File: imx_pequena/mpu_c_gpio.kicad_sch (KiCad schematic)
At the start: 1 part, among them U1 MCIMX6Z0DVM09AB

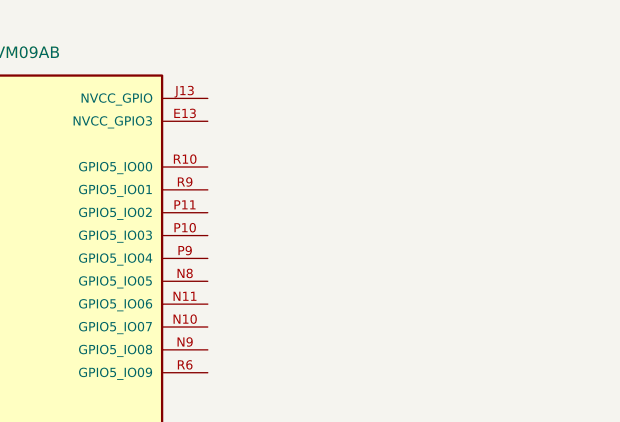
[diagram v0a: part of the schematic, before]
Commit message: Cleaned up NVCC pins
Added 3v3 connections + decoupling caps to NVcc pins
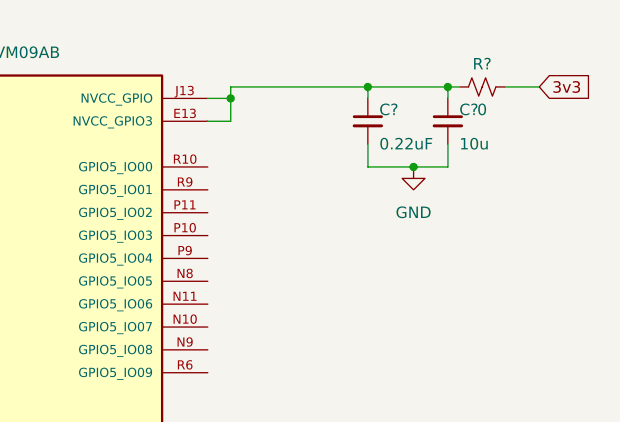
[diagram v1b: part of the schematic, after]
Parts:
- added C?: 10u, symbol Device:C_Small
- added C?: 0.22uF, symbol Device:C_Small
- added R?: 0, symbol Device:R_Small_US
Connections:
- net at U1.E13 (NVCC_GPIO3): now also U1.J13 (NVCC_GPIO), C?.1, C?.1, R?.1
- new net 3v3: R?.2
- new net GND: C?.2, C?.2
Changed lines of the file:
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@@
 (kicad_sch (version 20211123) (generator eeschema)
   (paper "A4")
+  (junction (at 185.42 48.26) (diameter 0) (color 0 0 0 0)
+  )
+  (junction (at 165.1 40.64) (diameter 0) (color 0 0 0 0)
+  )
+  (junction (at 180.34 39.37) (diameter 0) (color 0 0 0 0)
+  )
+  (junction (at 189.23 39.37) (diameter 0) (color 0 0 0 0)
+  )
+  (wire (pts (xy 189.23 39.37) (xy 189.23 40.64))
+    (stroke (width 0) (type default) (color 0 0 0 0))
+  )
+  (wire (pts (xy 165.1 40.64) (xy 165.1 39.37))
+    (stroke (width 0) (type default) (color 0 0 0 0))
+  )
+  (wire (pts (xy 165.1 39.37) (xy 180.34 39.37))
+    (stroke (width 0) (type default) (color 0 0 0 0))
+  )
+  (wire (pts (xy 165.1 43.18) (xy 165.1 40.64))
+    (stroke (width 0) (type default) (color 0 0 0 0))
+  )
+  (wire (pts (xy 189.23 45.72) (xy 189.23 48.26))
+    (stroke (width 0) (type default) (color 0 0 0 0))
+  )
+  (wire (pts (xy 180.34 39.37) (xy 189.23 39.37))
+    (stroke (width 0) (type default) (color 0 0 0 0))
+  )
+  (wire (pts (xy 180.34 45.72) (xy 180.34 48.26))
+    (stroke (width 0) (type default) (color 0 0 0 0))
+  )
+  (wire (pts (xy 189.23 39.37) (xy 190.5 39.37))
+    (stroke (width 0) (type default) (color 0 0 0 0))
+  )
+  (wire (pts (xy 185.42 48.26) (xy 189.23 48.26))
+    (stroke (width 0) (type default) (color 0 0 0 0))
+  )
+  (wire (pts (xy 162.56 40.64) (xy 165.1 40.64))
+    (stroke (width 0) (type default) (color 0 0 0 0))
+  )
+  (wire (pts (xy 180.34 39.37) (xy 180.34 40.64))
+    (stroke (width 0) (type default) (color 0 0 0 0))
+  )
+  (wire (pts (xy 180.34 48.26) (xy 185.42 48.26))
+    (stroke (width 0) (type default) (color 0 0 0 0))
+  )
+  (wire (pts (xy 195.58 39.37) (xy 199.39 39.37))
+    (stroke (width 0) (type default) (color 0 0 0 0))
+  )
+  (wire (pts (xy 162.56 43.18) (xy 165.1 43.18))
+    (stroke (width 0) (type default) (color 0 0 0 0))
+  )
+  (global_label "3v3" (shape input) (at 199.39 39.37 0) (fields_autoplaced)
+    (effects (font (size 1.27 1.27)) (justify left))
+    (property "Intersheet References" "${INTERSHEET_REFS}" (id 0) (at 205.1898 39.2906 0)
+      (effects (font (size 1.27 1.27)) (justify left) hide)
+    )
+  )
   (symbol (lib_id "MCIMX6Z0DVM09AB:MCIMX6Z0DVM09AB") (at 137.16 93.98 0) (unit 3)
     (in_bom yes) (on_board yes) (fields_autoplaced)
@@
     (pin "R9")
   )
+  (symbol (lib_id "Device:R_Small_US") (at 193.04 39.37 90) (unit 1)
+    (in_bom yes) (on_board yes)
+    (property "Reference" "R?" (id 0) (at 193.04 36.83 90))
+    (property "Value" "0" (id 1) (at 193.04 41.91 90))
+    (property "Footprint" "" (id 2) (at 193.04 39.37 0)
+      (effects (font (size 1.27 1.27)) hide)
+    )
+    (property "Datasheet" "~" (id 3) (at 193.04 39.37 0)
+      (effects (font (size 1.27 1.27)) hide)
+    )
+    (pin "1")
+    (pin "2")
+  )
+  (symbol (lib_id "power:GND") (at 185.42 48.26 0) (unit 1)
+    (in_bom yes) (on_board yes) (fields_autoplaced)
+    (property "Reference" "#PWR?" (id 0) (at 185.42 54.61 0)
+      (effects (font (size 1.27 1.27)) hide)
+    )
+    (property "Value" "GND" (id 1) (at 185.42 53.34 0))
+    (property "Footprint" "" (id 2) (at 185.42 48.26 0)
+      (effects (font (size 1.27 1.27)) hide)
+    )
+    (property "Datasheet" "" (id 3) (at 185.42 48.26 0)
+      (effects (font (size 1.27 1.27)) hide)
+    )
+    (pin "1")
+  )
+  (symbol (lib_id "Device:C_Small") (at 189.23 43.18 0) (unit 1)
+    (in_bom yes) (on_board yes)
+    (property "Reference" "C?" (id 0) (at 190.5 41.91 0)
+      (effects (font (size 1.27 1.27)) (justify left))
+    )
+    (property "Value" "10u" (id 1) (at 190.5 45.72 0)
+      (effects (font (size 1.27 1.27)) (justify left))
+    )
+    (property "Footprint" "" (id 2) (at 189.23 43.18 0)
+      (effects (font (size 1.27 1.27)) hide)
+    )
+    (property "Datasheet" "~" (id 3) (at 189.23 43.18 0)
+      (effects (font (size 1.27 1.27)) hide)
+    )
+    (pin "1")
+    (pin "2")
+  )
+  (symbol (lib_id "Device:C_Small") (at 180.34 43.18 0) (unit 1)
+    (in_bom yes) (on_board yes)
+    (property "Reference" "C?" (id 0) (at 181.61 41.91 0)
+      (effects (font (size 1.27 1.27)) (justify left))
+    )
+    (property "Value" "0.22uF" (id 1) (at 181.61 45.72 0)
+      (effects (font (size 1.27 1.27)) (justify left))
+    )
+    (property "Footprint" "" (id 2) (at 180.34 43.18 0)
+      (effects (font (size 1.27 1.27)) hide)
+    )
+    (property "Datasheet" "~" (id 3) (at 180.34 43.18 0)
+      (effects (font (size 1.27 1.27)) hide)
+    )
+    (pin "1")
+    (pin "2")
+  )
 )

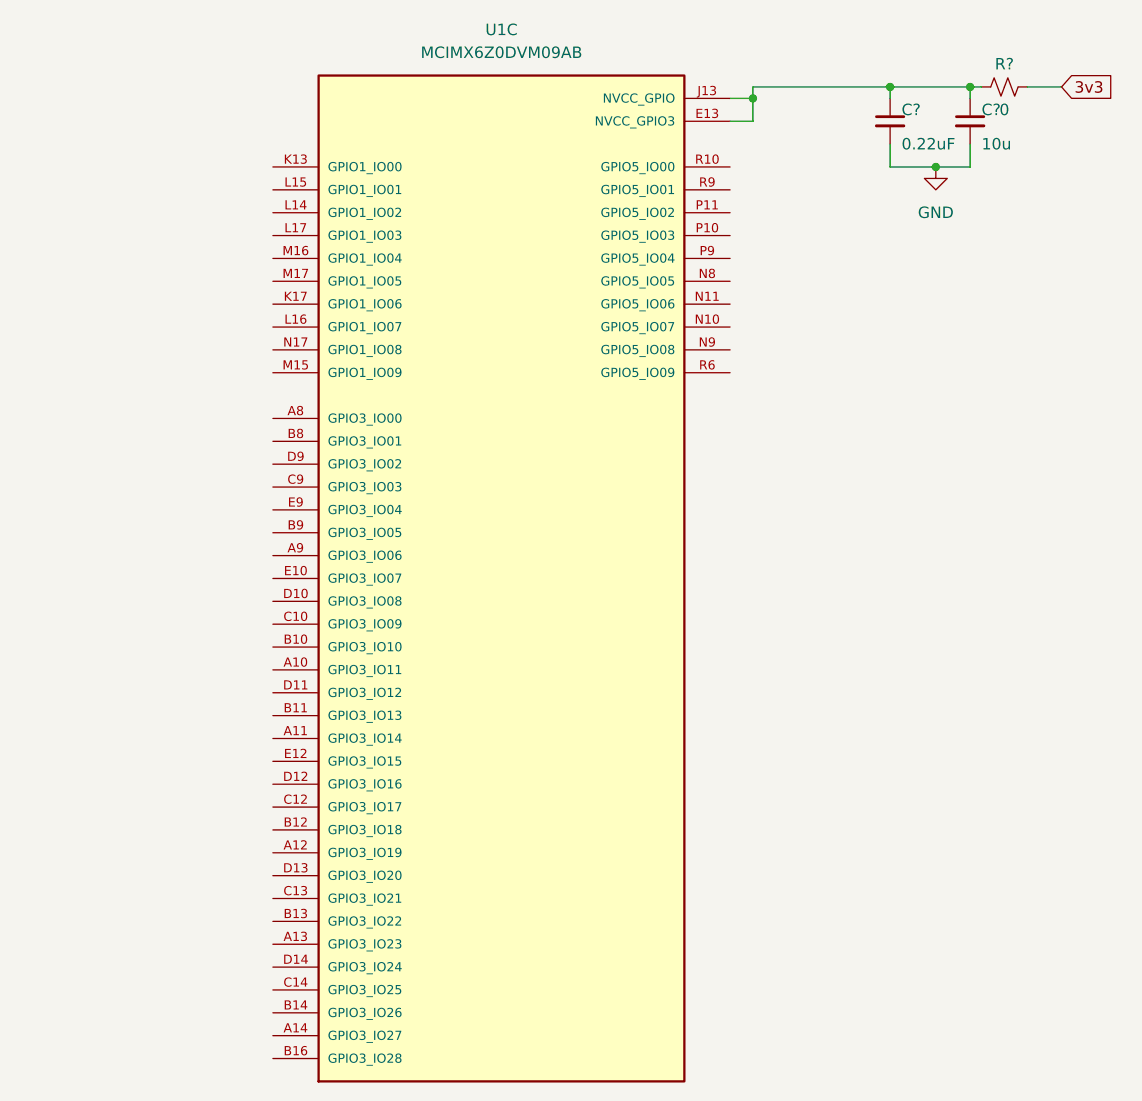
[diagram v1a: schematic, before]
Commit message: Pinout updates
Updated pinout files, changed pinout of gpio 1 and 3
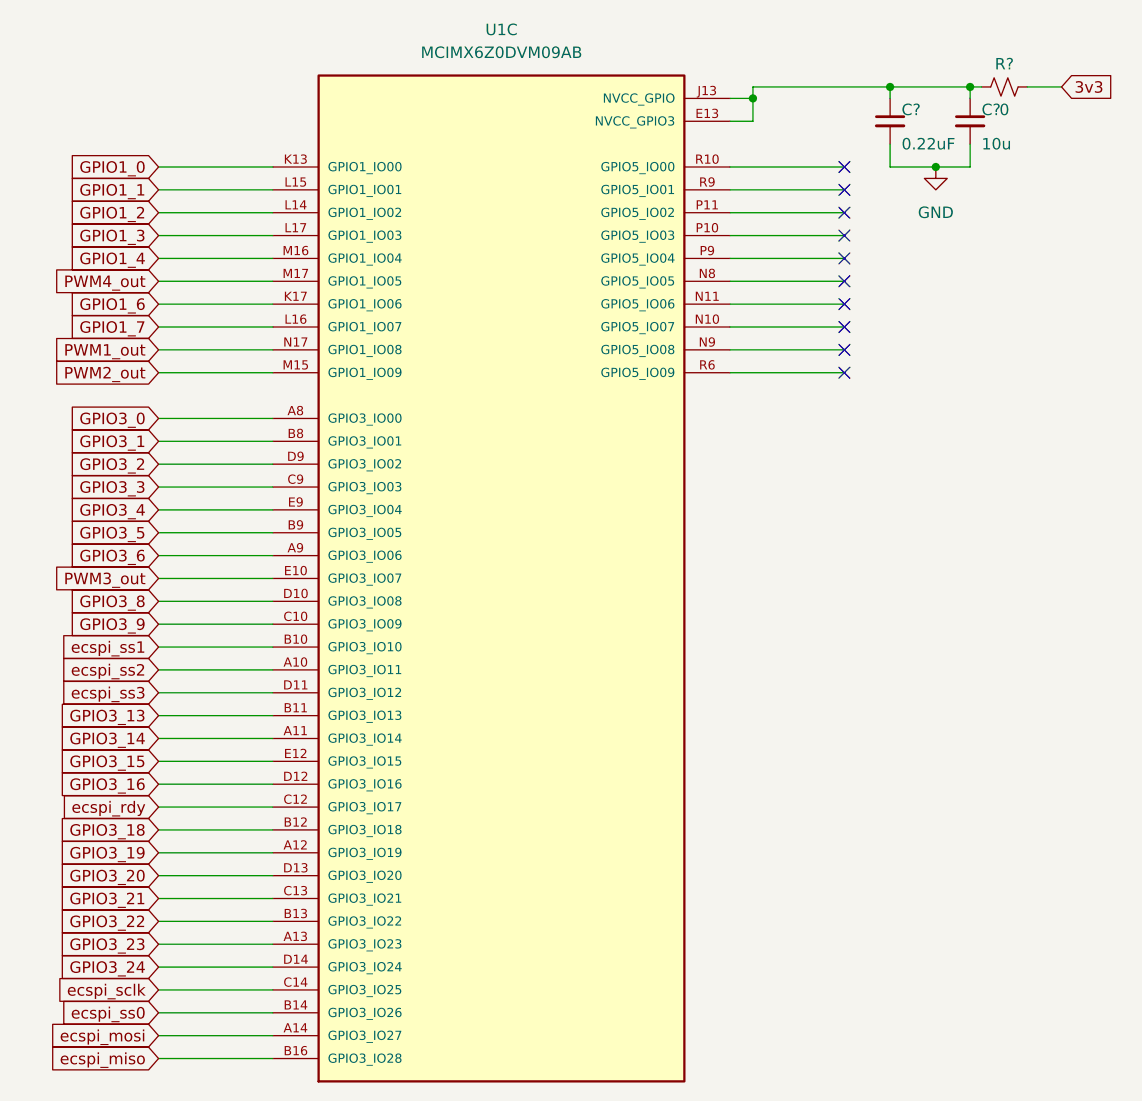
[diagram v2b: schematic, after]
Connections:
- net ecspi_ss2: now reaches U1.A10 (GPIO3_IO11)
- net GPIO3_14: now reaches U1.A11 (GPIO3_IO14)
- net GPIO3_19: now reaches U1.A12 (GPIO3_IO19)
- net GPIO3_23: now reaches U1.A13 (GPIO3_IO23)
- net ecspi_mosi: now reaches U1.A14 (GPIO3_IO27)
- net GPIO3_0: now reaches U1.A8 (GPIO3_IO00)
- net GPIO3_6: now reaches U1.A9 (GPIO3_IO06)
- net ecspi_ss1: now reaches U1.B10 (GPIO3_IO10)
- net GPIO3_13: now reaches U1.B11 (GPIO3_IO13)
- net GPIO3_18: now reaches U1.B12 (GPIO3_IO18)
- net GPIO3_22: now reaches U1.B13 (GPIO3_IO22)
- net ecspi_ss0: now reaches U1.B14 (GPIO3_IO26)
- net ecspi_miso: now reaches U1.B16 (GPIO3_IO28)
- net GPIO3_1: now reaches U1.B8 (GPIO3_IO01)
- net GPIO3_5: now reaches U1.B9 (GPIO3_IO05)
- net GPIO3_9: now reaches U1.C10 (GPIO3_IO09)
- net ecspi_rdy: now reaches U1.C12 (GPIO3_IO17)
- net GPIO3_21: now reaches U1.C13 (GPIO3_IO21)
- net ecspi_sclk: now reaches U1.C14 (GPIO3_IO25)
- net GPIO3_3: now reaches U1.C9 (GPIO3_IO03)
- net GPIO3_8: now reaches U1.D10 (GPIO3_IO08)
- net ecspi_ss3: now reaches U1.D11 (GPIO3_IO12)
- net GPIO3_16: now reaches U1.D12 (GPIO3_IO16)
- net GPIO3_20: now reaches U1.D13 (GPIO3_IO20)
- net GPIO3_24: now reaches U1.D14 (GPIO3_IO24)
- net GPIO3_2: now reaches U1.D9 (GPIO3_IO02)
- net PWM3_out: now reaches U1.E10 (GPIO3_IO07)
- net GPIO3_15: now reaches U1.E12 (GPIO3_IO15)
- net GPIO3_4: now reaches U1.E9 (GPIO3_IO04)
- net GPIO1_0: now reaches U1.K13 (GPIO1_IO00)
- net GPIO1_6: now reaches U1.K17 (GPIO1_IO06)
- net GPIO1_2: now reaches U1.L14 (GPIO1_IO02)
- net GPIO1_1: now reaches U1.L15 (GPIO1_IO01)
- net GPIO1_7: now reaches U1.L16 (GPIO1_IO07)
- net GPIO1_3: now reaches U1.L17 (GPIO1_IO03)
- net PWM2_out: now reaches U1.M15 (GPIO1_IO09)
- net GPIO1_4: now reaches U1.M16 (GPIO1_IO04)
- net PWM4_out: now reaches U1.M17 (GPIO1_IO05)
- net PWM1_out: now reaches U1.N17 (GPIO1_IO08)
- no-connect marks 0 -> 10

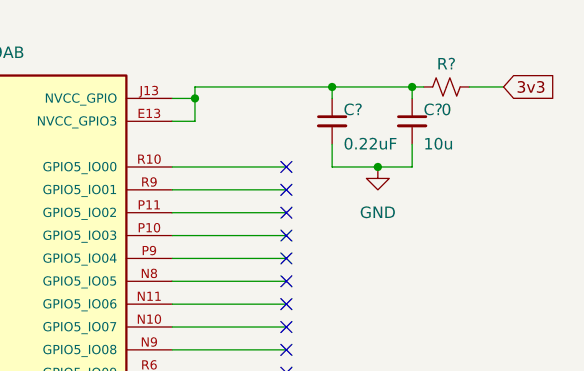
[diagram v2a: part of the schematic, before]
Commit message: Part Assignment
Assigned GPIOs and assigned footprints to most parts
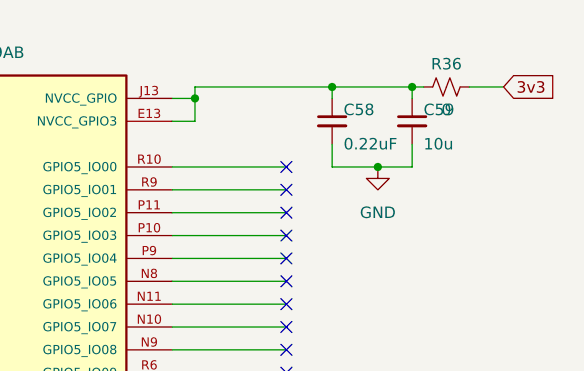
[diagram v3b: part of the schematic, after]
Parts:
- C58: renamed from C?; footprint (none) -> Capacitor_SMD:C_0402_1005Metric
- C59: renamed from C?; footprint (none) -> Capacitor_SMD:C_0805_2012Metric
- R36: renamed from R?; footprint (none) -> Resistor_SMD:R_0402_1005Metric
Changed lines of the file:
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@@
   (symbol (lib_id "Device:R_Small_US") (at 193.04 39.37 90) (unit 1)
     (in_bom yes) (on_board yes)
-    (property "Reference" "R?" (id 0) (at 193.04 36.83 90))
+    (property "Reference" "R36" (id 0) (at 193.04 36.83 90))
     (property "Value" "0" (id 1) (at 193.04 41.91 90))
-    (property "Footprint" "" (id 2) (at 193.04 39.37 0)
+    (property "Footprint" "Resistor_SMD:R_0402_1005Metric" (id 2) (at 193.04 39.37 0)
       (effects (font (size 1.27 1.27)) hide)
     )
@@
   (symbol (lib_id "power:GND") (at 185.42 48.26 0) (unit 1)
     (in_bom yes) (on_board yes) (fields_autoplaced)
-    (property "Reference" "#PWR?" (id 0) (at 185.42 54.61 0)
+    (property "Reference" "#PWR0150" (id 0) (at 185.42 54.61 0)
       (effects (font (size 1.27 1.27)) hide)
     )
@@
   (symbol (lib_id "Device:C_Small") (at 189.23 43.18 0) (unit 1)
     (in_bom yes) (on_board yes)
-    (property "Reference" "C?" (id 0) (at 190.5 41.91 0)
+    (property "Reference" "C59" (id 0) (at 190.5 41.91 0)
       (effects (font (size 1.27 1.27)) (justify left))
     )
@@
       (effects (font (size 1.27 1.27)) (justify left))
     )
-    (property "Footprint" "" (id 2) (at 189.23 43.18 0)
+    (property "Footprint" "Capacitor_SMD:C_0805_2012Metric" (id 2) (at 189.23 43.18 0)
       (effects (font (size 1.27 1.27)) hide)
     )
@@
   (symbol (lib_id "Device:C_Small") (at 180.34 43.18 0) (unit 1)
     (in_bom yes) (on_board yes)
-    (property "Reference" "C?" (id 0) (at 181.61 41.91 0)
+    (property "Reference" "C58" (id 0) (at 181.61 41.91 0)
       (effects (font (size 1.27 1.27)) (justify left))
     )
@@
       (effects (font (size 1.27 1.27)) (justify left))
     )
-    (property "Footprint" "" (id 2) (at 180.34 43.18 0)
+    (property "Footprint" "Capacitor_SMD:C_0402_1005Metric" (id 2) (at 180.34 43.18 0)
       (effects (font (size 1.27 1.27)) hide)
     )
